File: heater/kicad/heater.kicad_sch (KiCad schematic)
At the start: 82 parts, among them J1 Conn_01x02_Pin, J2 Conn_01x02_Pin, J3 pcie_98, U1 OPA863SIDBVR, U10 B0509XT-1WR3, U11 ESD5344D-TP, U12 ESD5344D-TP, U13 XC6206P332MR, U2 OPA863SIDBVR, U3 LTC1968, U4 LTC1968, U5 OPA863SIDBVR, U6 OPA863SIDBVR, U7 LP2985-5.0, U8 ADS1115IDGS, U9 ISO1541

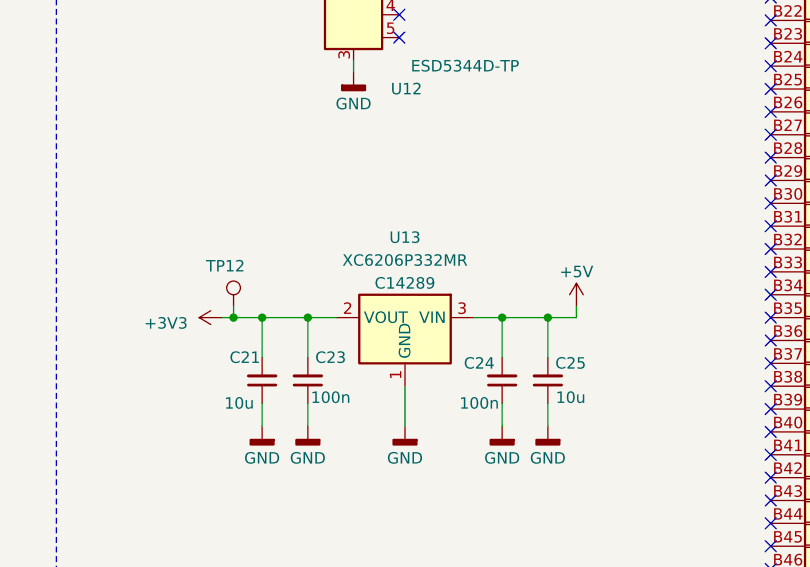
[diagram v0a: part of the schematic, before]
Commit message: Adjusted for JLCPCB upload.
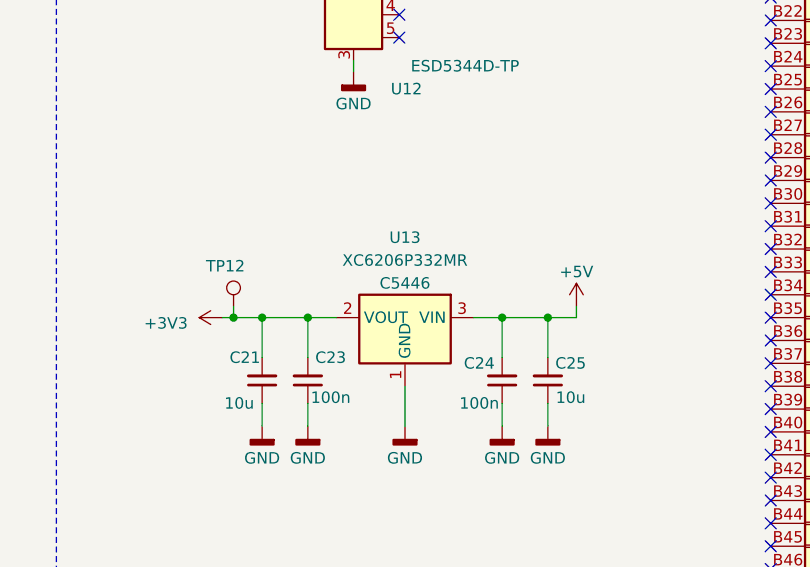
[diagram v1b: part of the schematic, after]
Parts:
- U10: JLCRotOffset (none) -> 270; LCSC (none) -> C976389
- U13: JLCRotOffset (none) -> 180; LCSC C14289 -> C5446
- U7: JLCRotOffset (none) -> 180
- U8: LCSC (none) -> Digikey
- U9: JLCRotOffset (none) -> 270
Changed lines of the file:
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@@
+      (effects (font (size 1.27 1.27)) hide)
+    )
+    (property "LCSC" "Digikey" (at 196.85 63.5 0)
       (effects (font (size 1.27 1.27)) hide)
     )
@@
       (effects (font (size 1.27 1.27)) hide)
     )
+    (property "JLCRotOffset" "270" (at 255.27 62.23 0)
+      (effects (font (size 1.27 1.27)) hide)
+    )
     (pin "1")
     (pin "2")
@@
       (effects (font (size 1.27 1.27)) hide)
     )
+    (property "JLCRotOffset" "180" (at 192.405 196.215 0)
+      (effects (font (size 1.27 1.27)) hide)
+    )
     (pin "1")
     (pin "2")
@@
       (effects (font (size 1.27 1.27)) hide)
     )
-    (property "LCSC" "C14289" (at 294.005 134.62 0)
-      (effects (font (size 1.27 1.27)))
+    (property "LCSC" "C5446" (at 294.005 134.62 0)
+      (effects (font (size 1.27 1.27)))
+    )
+    (property "JLCRotOffset" "180" (at 294.005 140.97 0)
+      (effects (font (size 1.27 1.27)) hide)
     )
     (pin "1")
@@
       (effects (font (size 1.27 1.27)) hide)
     )
+    (property "LCSC" "C976389" (at 255.27 196.85 0)
+      (effects (font (size 1.27 1.27)) hide)
+    )
+    (property "JLCRotOffset" "270" (at 255.27 196.85 0)
+      (effects (font (size 1.27 1.27)) hide)
+    )

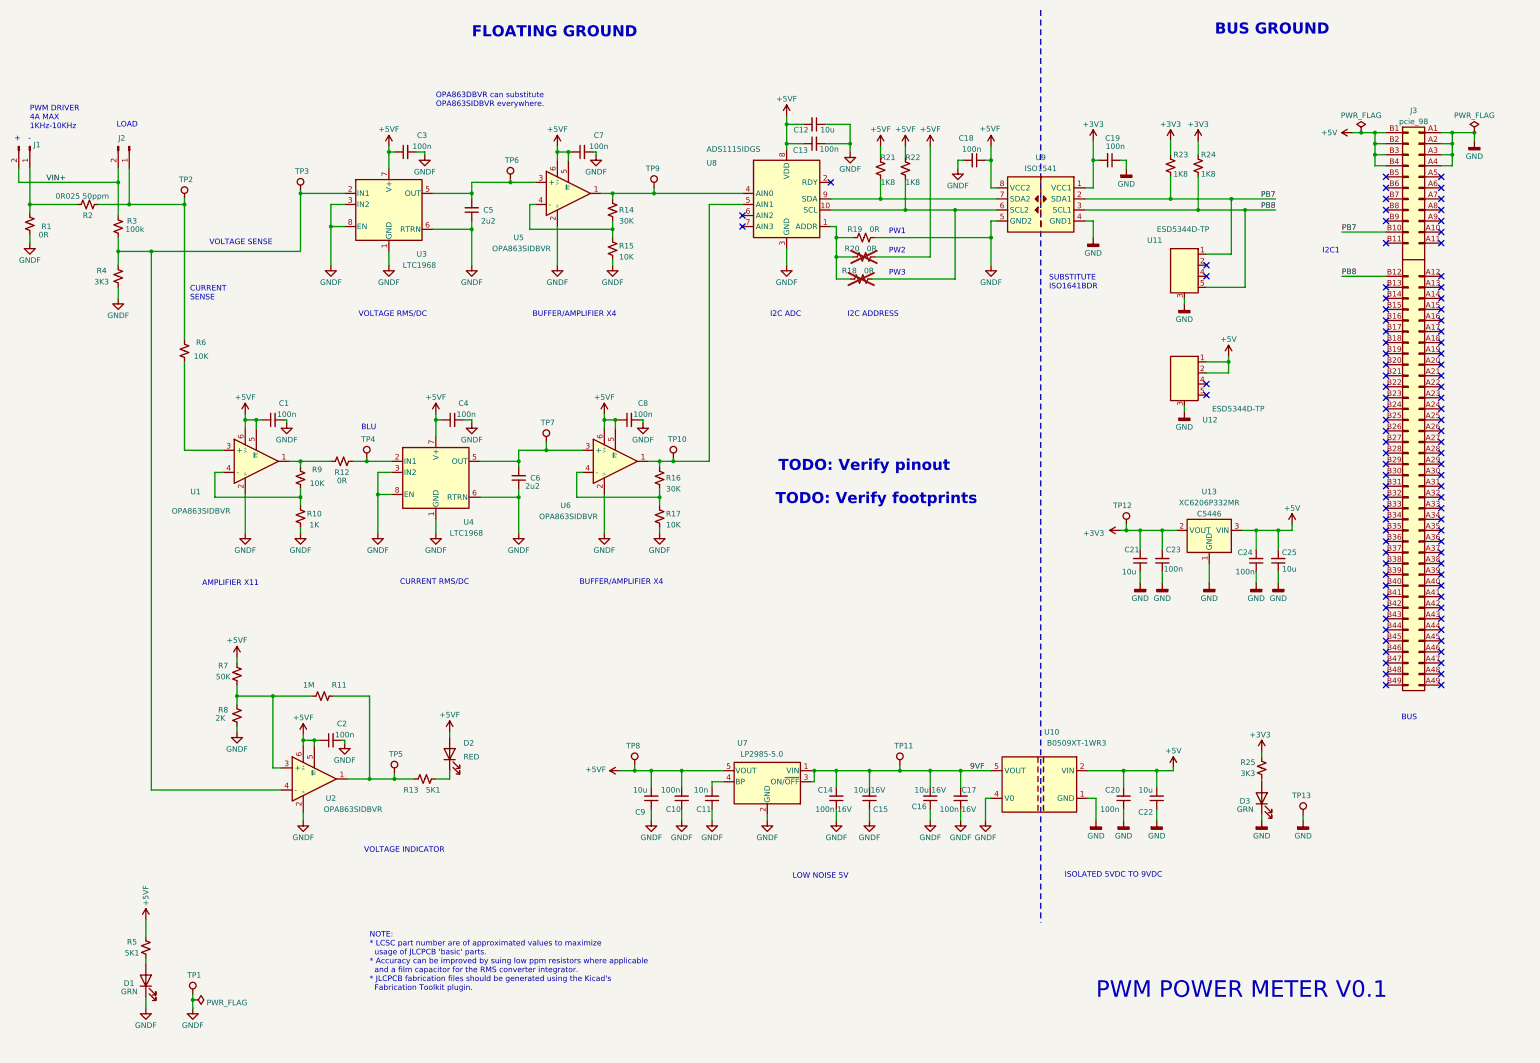
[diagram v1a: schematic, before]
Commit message: Routed V2 of the heater board.
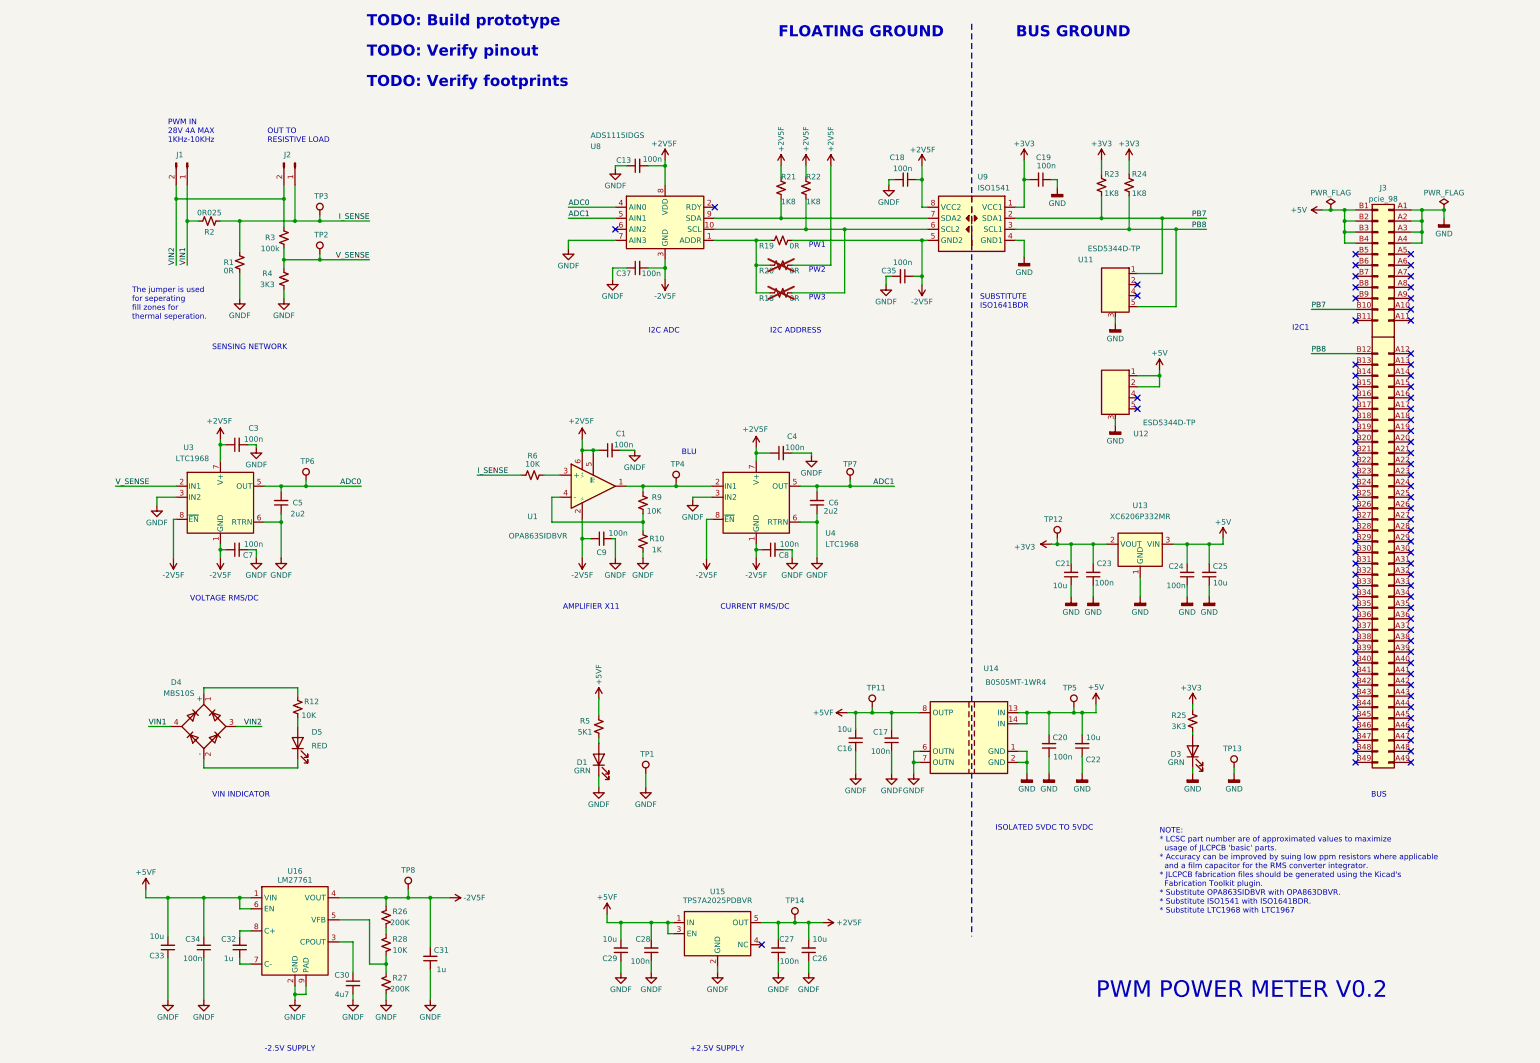
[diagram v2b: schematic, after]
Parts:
- removed C10, C2: 100n, Capacitor_SMD:C_0402_1005Metric, symbol Device:C_Small
- removed C11: 10n, Capacitor_SMD:C_0402_1005Metric, symbol Device:C_Small
- removed C12: 10u, Capacitor_SMD:C_0603_1608Metric, symbol Device:C_Small
- removed C14: 100n 16V, Capacitor_SMD:C_0402_1005Metric, symbol Device:C_Small
- removed C15: 10u 16V, Capacitor_SMD:C_0603_1608Metric, symbol Device:C_Small
- removed D2: RED, LED_SMD:LED_0603_1608Metric, symbol Device:LED
- removed R11: 1M, Resistor_SMD:R_0402_1005Metric, symbol Device:R_Small_US
- removed R13: 5K1, Resistor_SMD:R_0402_1005Metric, symbol Device:R_Small_US
- removed R14, R16: 30K, Resistor_SMD:R_0402_1005Metric, symbol Device:R_Small_US
- removed R15, R17: 10K, Resistor_SMD:R_0402_1005Metric, symbol Device:R_Small_US
- removed R7: 50K, Resistor_SMD:R_0402_1005Metric, symbol Device:R_Small_US
- removed R8: 2K, Resistor_SMD:R_0402_1005Metric, symbol Device:R_Small_US
- removed TP10, TP9: TestPoint, common:Test_Pad, symbol common:TestPoint
- removed U10: B0509XT-1WR3, heater:Converter_DCDC, symbol heater:B0509XT
- removed U2, U5, U6: OPA863SIDBVR, Package_TO_SOT_SMD:TSOT-23-6, symbol heater:OPA863SIDBVR
- removed U7: LP2985-5.0, Package_TO_SOT_SMD:SOT-23-5, symbol Regulator_Linear:LP2985-5.0
- added C26, C29, C33: 10u, Capacitor_SMD:C_0603_1608Metric, symbol Device:C_Small
- added C27, C28, C34, C35, C37: 100n, Capacitor_SMD:C_0402_1005Metric, symbol Device:C_Small
- added C30: 4u7, Capacitor_SMD:C_0603_1608Metric, symbol Device:C_Small
- added C31, C32: 1u, Capacitor_SMD:C_0402_1005Metric, symbol Device:C_Small
- added D4: MBS10S, common:Diode_Bridge_MBS10, symbol Diode_Bridge:ABS10
- added D5: RED, LED_SMD:LED_0603_1608Metric, symbol Device:LED
- added R26, R27: 200K, Resistor_SMD:R_0402_1005Metric, symbol Device:R_Small_US
- added R28: 10K, Resistor_SMD:R_0402_1005Metric, symbol Device:R_Small_US
- added TP14: TestPoint, common:Test_Pad, symbol common:TestPoint
- added U14: B0505MT-1WR4, common:B0505MT-1WR4, symbol common:B0505MT-1WR4
- added U15: TPS7A2025PDBVR, Package_TO_SOT_SMD:SOT-23-5, symbol common:TPS7A2025PDBVR
- added U16: LM27761, Package_SON:WSON-8-1EP_2x2mm_P0.5mm_EP0.9x1.6mm, symbol Regulator_SwitchedCapacitor:LM27761
- C16: value 10u 16V -> 10u; LCSC C96446 -> C19702
- C17: value 100n 16V -> 100n
- C9: value 10u -> 100n; footprint Capacitor_SMD:C_0603_1608Metric -> Capacitor_SMD:C_0402_1005Metric; LCSC C19702 -> C1525
- R12: value 0R -> 10K; LCSC C17168 -> C25744
- R2: value 0R025 50ppm -> 0R025
- U9: LCSC (none) -> ISO1541DR
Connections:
- net 9VF is gone; now on net +5VF: C16.2, C17.2, TP11.1
- net +5V: now also TP5.1, U14.13 (IN), U14.14 (IN)
- net +5VF: now also C28.2, C29.2, C33.2, C34.2, U14.8 (OUTP), U15.1 (IN), U15.3 (EN), U16.1 (VIN), U16.6 (EN); no longer C1.1, C13.1, C18.1, C3.1, C4.1, C7.1, C8.1, C9.2, R20.2, R21.2, R22.2, TP8.1, U1.5 (~{PD}), U1.6 (V+), U3.7 (V+), U4.7 (V+), U8.8 (VDD), U9.8 (VCC2)
- net GND: now also U14.1 (GND), U14.2 (GND)
- net GNDF: now also C13.1, C9.2, U8.7 (AIN3), C26.1, C27.1, C28.1, C29.1, C30.2, C31.1, C33.1, C34.1, C35.2, C37.1, R27.2, U14.6 (OUTN), U14.7 (OUTN), U15.2 (GND), U16.2 (GND), U16.9 (PAD); no longer C13.2, C9.1, R19.2, U1.2 (V-), U3.1 (GND), U3.8 (EN), U4.1 (GND), U4.8 (EN), U8.3 (GND), U9.5 (GND2)
- net ADC0: now reaches C5.2, TP6.1, U3.5 (OUT)
- net ADC0: now also U8.4 (AIN0)
- net at R9.1, U1.1: now also TP4.1, U4.2 (IN1); no longer R12.2
- net ADC1: now reaches C6.2, TP7.1, U4.5 (OUT)
- net ADC1: now also U8.5 (AIN1)
- net V_SENSE: now reaches R3.1, R4.1, U3.2 (IN1)
- net V_SENSE: now also TP2.1; no longer TP3.1
- net I_SENSE: now reaches J2.1 (Pin_1), R2.2, R6.1
- net I_SENSE: now also R1.1, TP3.1; no longer TP2.1
- net VIN1: now reaches J1.1 (Pin_1), R2.1
- net VIN1: now also D4.4; no longer R1.1
- net VIN+ renamed VIN2
- net VIN2: now also D4.3
- new net: C32.1, U16.7 (C-)
- new net: C32.2, U16.8 (C+)
- new net: C30.1, U16.3 (CPOUT)
- new net: D4.1 (+), R12.1
- new net: D4.2 (-), D5.1 (K)
- new net: R27.1, R28.2, U16.5 (VFB)
- new net: D5.2 (A), R12.2
- new net: R26.2, R28.1
- new net +2V5F: C1.1, C13.2, C18.1, C26.2, C27.2, C3.1, C4.1, R20.2, R21.2, R22.2, TP14.1, U1.5 (~{PD}), U1.6 (V+), U15.5 (OUT), U3.7 (V+), U4.7 (V+), U8.8 (VDD), U9.8 (VCC2)
- new net -2V5F: C31.2, C35.1, C37.2, C7.1, C8.1, C9.1, R19.2, R26.1, TP8.1, U1.2 (V-), U16.4 (VOUT), U3.1 (GND), U3.8 (~{EN}), U4.1 (GND), U4.8 (~{EN}), U8.3 (GND), U9.5 (GND2)
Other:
- note added: "+2.5V SUPPLY"
- note added: "-2.5V SUPPLY"
- note added: "ISOLATED 5VDC TO 5VDC"
- note added: "NOTE: * LCSC part number are of approximated values to maximize usage of JLCPCB 'basic' parts. * Accuracy can be improved by suing low ppm resistors where applicable and a film capacitor for the RMS converter integrator. * JLCPCB fabrication files should be generated using the Kicad's Fabrication Toolkit plugin. * Substitute OPA863SIDBVR with OPA863DBVR. * Substitute ISO1541 with ISO1641BDR. * Su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"
- note added: "OUT TO RESISTIVE LOAD"
- note added: "PWM IN 28V 4A MAX 1KHz-10KHz"
- note added: "PWM POWER METER V0.2"
- note added: "SENSING NETWORK"
- note added: "TODO: Build prototype"
- note added: "The jumper is used for seperating fill zones for thermal seperation."
- note added: "VIN INDICATOR"
- note removed: "+"
- note removed: "-"
- note removed: "BUFFER/AMPLIFIER X4"
- note removed: "CURRENT SENSE"
- note removed: "ISOLATED 5VDC TO 9VDC"
- note removed: "LOAD"
- note removed: "LOW NOISE 5V"
- note removed: "NOTE: * LCSC part number are of approximated values to maximize usage of JLCPCB 'basic' parts. * Accuracy can be improved by suing low ppm resistors where applicable and a film capacitor for the RMS converter integrator. * JLCPCB fabrication files should be generated using the Kicad's Fabrication Toolkit plugin."
- note removed: "OPA863DBVR can substitute OPA863SIDBVR everywhere."
- note removed: "PWM DRIVER 4A MAX 1KHz-10KHz"
- note removed: "PWM POWER METER V0.1"
- note removed: "VOLTAGE INDICATOR"
- note removed: "VOLTAGE SENSE"
- moved on the sheet: C1, C13, C16, C17, C18, C19, C20, C21, C22, C23, C24, C25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

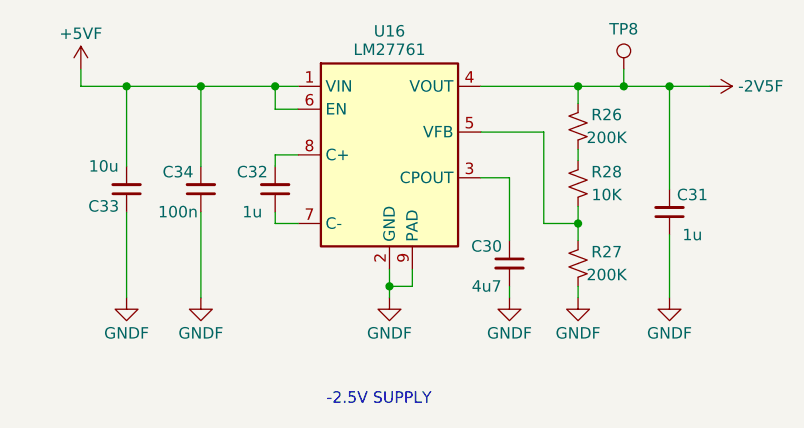
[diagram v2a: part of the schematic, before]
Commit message: Updated heater schematic.
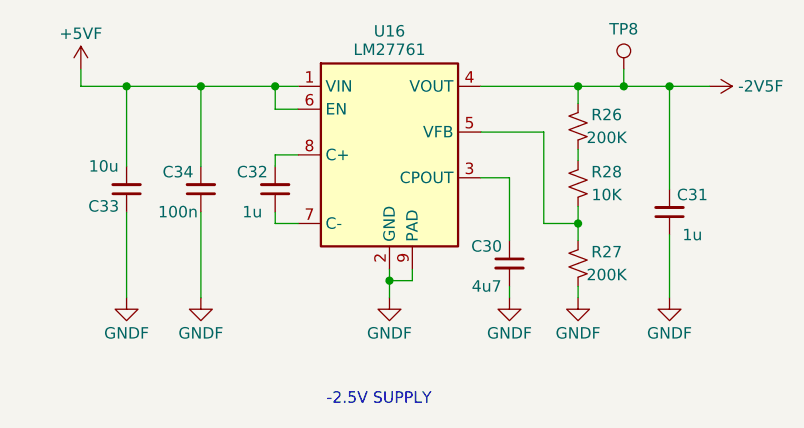
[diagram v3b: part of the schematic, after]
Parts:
- C30: footprint Capacitor_SMD:C_0603_1608Metric -> Capacitor_SMD:C_0402_1005Metric; LCSC C19666 -> C23733
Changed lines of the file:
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@@
   (junction (at 189.865 142.875) (diameter 0) (color 0 0 0 0)
   )
+  (junction (at 83.82 244.475) (diameter 0) (color 0 0 0 0)
+  )
   (junction (at 220.98 180.34) (diameter 0) (color 0 0 0 0)
   )
@@
   )
   (junction (at 262.255 141.605) (diameter 0) (color 0 0 0 0)
-  )
-  (junction (at 83.82 245.11) (diameter 0) (color 0 0 0 0)
   )
   (junction (at 114.935 222.885) (diameter 0) (color 0 0 0 0)
@@
     (stroke (width 0) (type default))
   )
-  (wire (pts (xy 86.36 245.11) (xy 83.82 245.11))
+  (wire (pts (xy 86.36 244.475) (xy 83.82 244.475))
     (stroke (width 0) (type default))
   )
@@
     (stroke (width 0) (type default))
   )
+  (wire (pts (xy 83.82 244.475) (xy 83.82 246.38))
+    (stroke (width 0) (type default))
+  )
   (wire (pts (xy 189.865 83.82) (xy 193.04 83.82))
     (stroke (width 0) (type default))
@@
     (stroke (width 0) (type default))
   )
-  (wire (pts (xy 83.82 243.205) (xy 83.82 245.11))
+  (wire (pts (xy 83.82 243.205) (xy 83.82 244.475))
     (stroke (width 0) (type default))
   )
@@
     (stroke (width 0) (type default))
   )
-  (wire (pts (xy 83.82 245.11) (xy 83.82 246.38))
-    (stroke (width 0) (type default))
-  )
   (wire (pts (xy 198.755 228.6) (xy 201.93 228.6))
     (stroke (width 0) (type default))
@@
     (stroke (width 0) (type default))
   )
-  (wire (pts (xy 86.36 243.205) (xy 86.36 245.11))
+  (wire (pts (xy 86.36 243.205) (xy 86.36 244.475))
     (stroke (width 0) (type default))
   )
@@
       (effects (font (size 1.27 1.27)))
     )
-    (property "Footprint" "Capacitor_SMD:C_0603_1608Metric" (at 97.155 242.57 0)
+    (property "Footprint" "Capacitor_SMD:C_0402_1005Metric" (at 97.155 242.57 0)
       (effects (font (size 1.27 1.27)) hide)
     )
@@
       (effects (font (size 1.27 1.27)) hide)
     )
-    (property "LCSC" "C19666" (at 97.155 242.57 0)
-      (effects (font (size 1.27 1.27)) hide)
-    )
+    (property "LCSC" "C23733" (at 97.155 242.57 0)
+      (effects (font (size 1.27 1.27)) hide)
+    )
